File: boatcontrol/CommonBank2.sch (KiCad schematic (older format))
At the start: 29 parts, among them J5101 Conn_01x01_Male, J5102 TBP01R2W-508-08BE, J5103 Conn_01x01_Male, J5104 TBL008V-1000-02BE, J5105 TBP01R2W-508-08BE, J5106 Conn_01x01_Male, J5107 Conn_01x01_Male, J5108 TBL008V-1000-02BE, Q5101 IPP120P04P4L-03, U5101 MCP23017-E/SP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

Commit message: RPi scheme update done
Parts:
- JP5109, JP5110: value Jumper_NO_Small -> Jumper_NC_Small; symbol Device:Jumper_NO_Small -> Device:Jumper_NC_Small
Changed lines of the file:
@@
 Connection ~ 8150 2400
 $Comp
-L Device:Jumper_NO_Small JP?
+L Device:Jumper_NC_Small JP?
 U 1 1 61788453
 P 9600 5850
@@
 AR Path="/D1BB8DB4/61788453" Ref="JP5110"  Part="1"
 F 0 "JP5110" H 9600 5950 50  0000 C CNN
-F 1 "Jumper_NO_Small" H 9650 5750 50  0001 C CNN
+F 1 "Jumper_NC_Small" H 9650 5750 50  0001 C CNN
 F 2 "Connector_PinHeader_2.54mm:PinHeader_1x02_P2.54mm_Vertical" H 9600 5850 50  0001 C CNN
 F 3 "~" H 9600 5850 50  0001 C CNN
@@
 	9750 5850 9750 6000
 $Comp
-L Device:Jumper_NO_Small JP?
+L Device:Jumper_NC_Small JP?
 U 1 1 617AACB3
 P 9500 2150
@@
 AR Path="/D1BB8DB4/617AACB3" Ref="JP5109"  Part="1"
 F 0 "JP5109" H 9500 2250 50  0000 C CNN
-F 1 "Jumper_NO_Small" H 9550 2050 50  0001 C CNN
+F 1 "Jumper_NC_Small" H 9550 2050 50  0001 C CNN
 F 2 "Connector_PinHeader_2.54mm:PinHeader_1x02_P2.54mm_Vertical" H 9500 2150 50  0001 C CNN
 F 3 "~" H 9500 2150 50  0001 C CNN
@@
 Wire Wire Line
 	9600 2150 9650 2150
-Text Notes 7400 1100 0    50   ~ 0
-It's safe to run AC up to 277V 50/60hz and DC up to 24V on this circuit even though it's marked AC.\nThe main difference between this and the DC specific circuits  is track spacing and lack of any polarity protection.
+Text Notes 6700 850  0    50   ~ 0
+It's safe to run AC up to 277V 50/60hz and DC up to 24V on this circuit even though it's marked AC.\nThe main difference between this and the DC specific circuits is track spacing and lack of any polarity protection.
 $Comp
 L BoatControl:TBL008V-1000-02BE J?

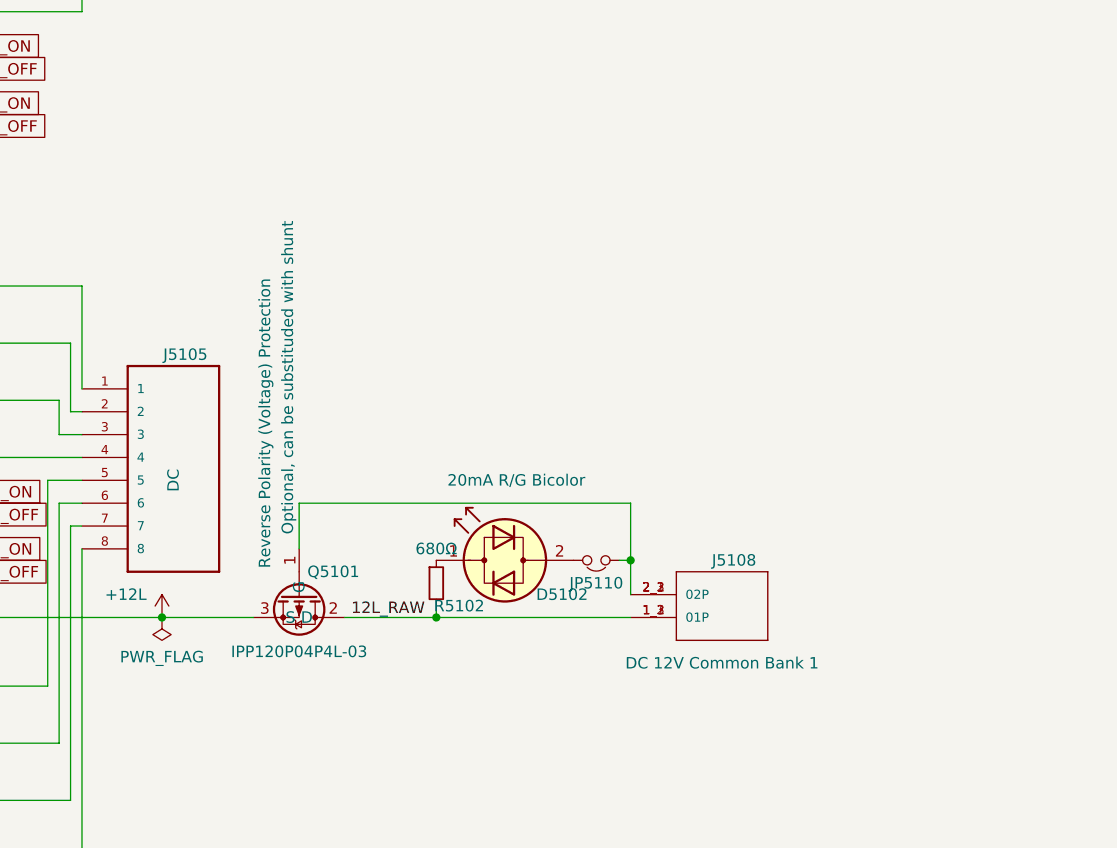
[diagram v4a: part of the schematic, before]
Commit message: Scale reverse polarity protection
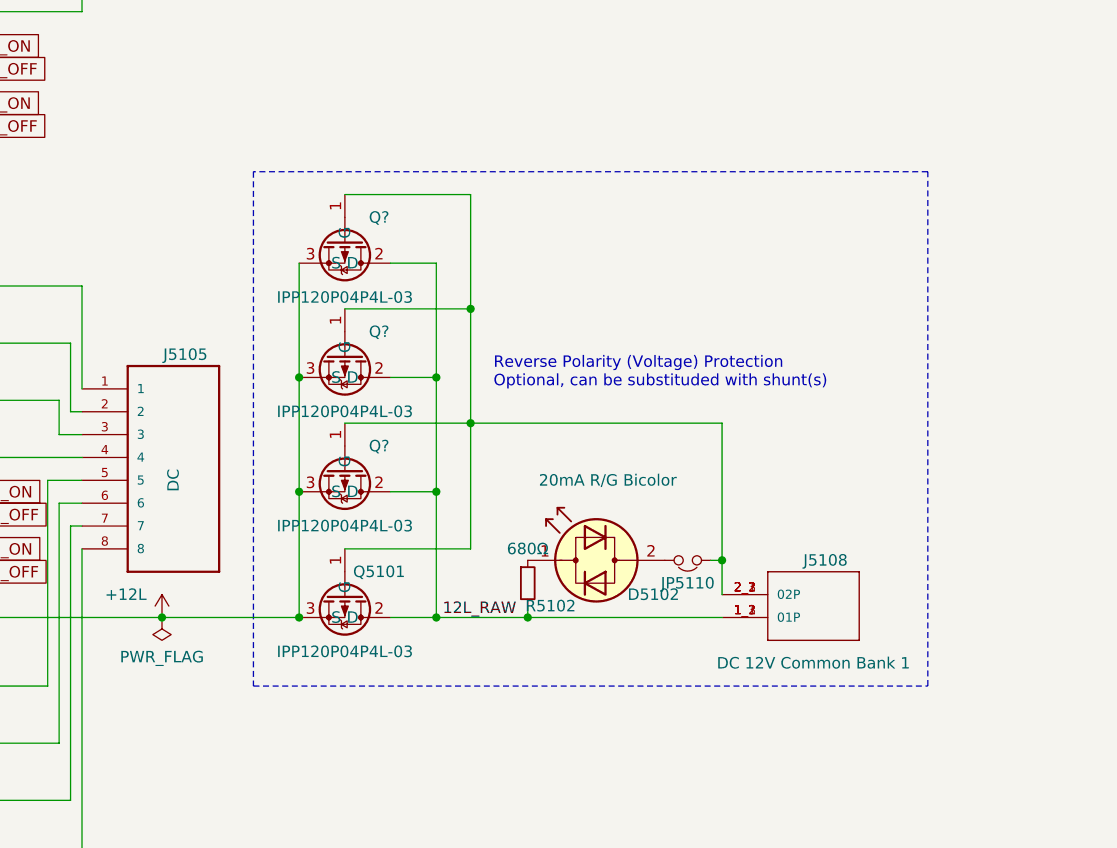
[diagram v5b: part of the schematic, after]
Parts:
- added Q? (x3): IPP120P04P4L-03, Package_TO_SOT_THT:TO-220-3_Vertical, symbol BoatControl:IPP120P04P4L-03
- Q5101: Note Optional, can be substituded with shunt -> (none); Purpose Reverse Polarity (Voltage) Protection -> (none)
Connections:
- net +12L: now also Q?.3 (S), Q?.3 (S), Q?.3 (S)
- net 12L_RAW: now also Q?.2 (D), Q?.2 (D), Q?.2 (D)
- net at J5108.2_1 (02P), J5108.2_2 (02P), J5108.2_3 (02P)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: now also Q?.1 (G), Q?.1 (G), Q?.1 (G)
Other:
- note added: "Reverse Polarity (Voltage) Protection\nOptional, can be substituded with shunt(s)"
- moved on the sheet: D5102, J5108, JP5110, Q5101, R5102

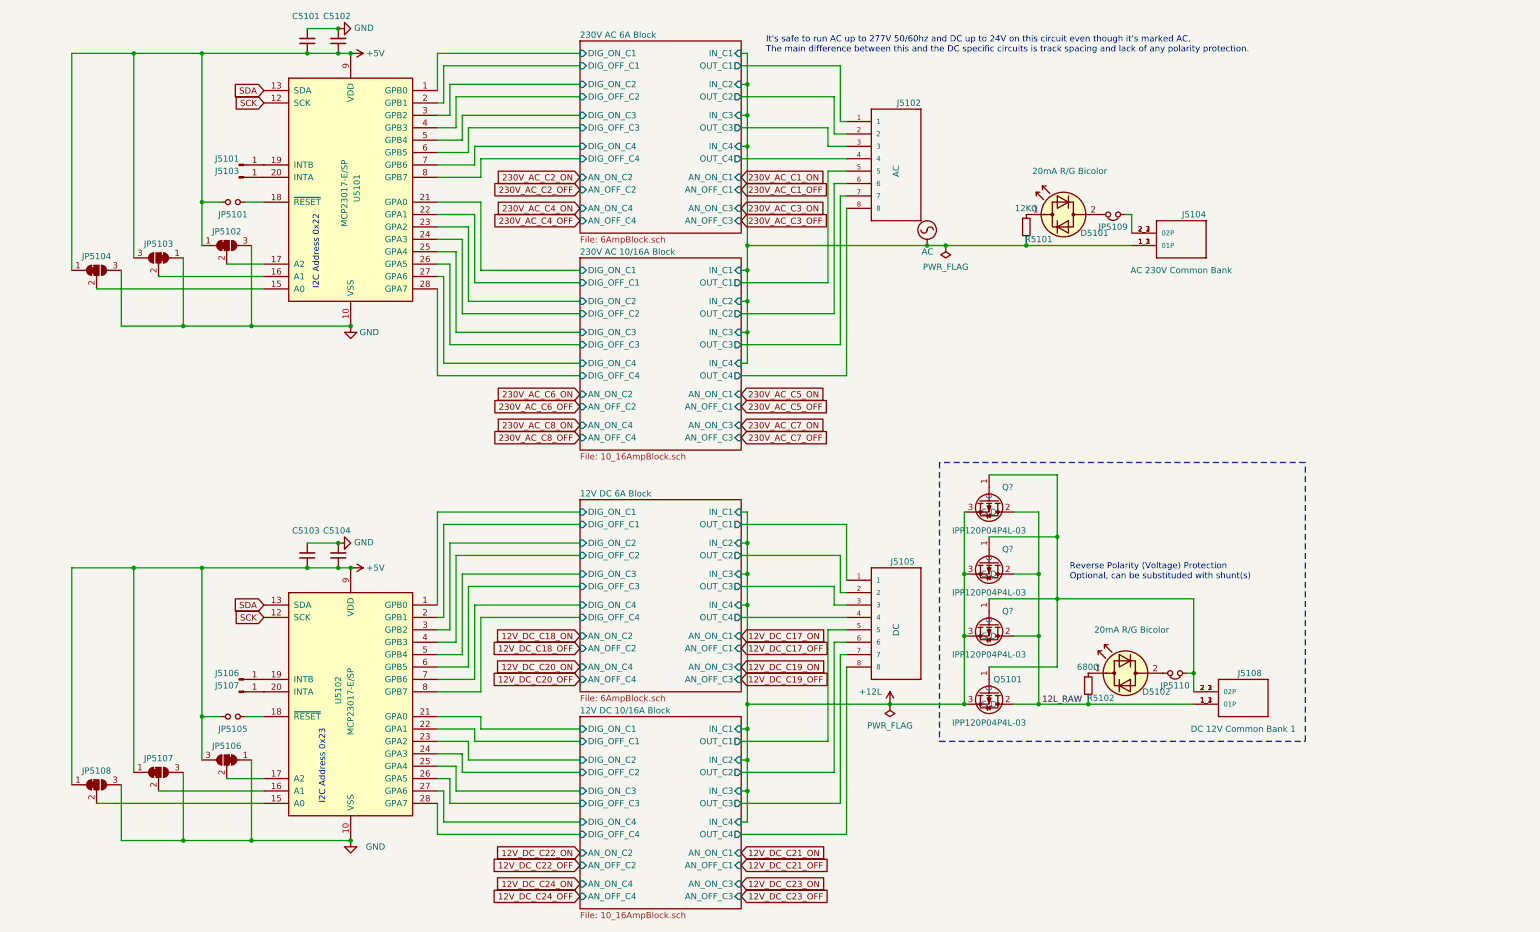
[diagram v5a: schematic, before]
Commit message: Add notes about power use of polarity protection
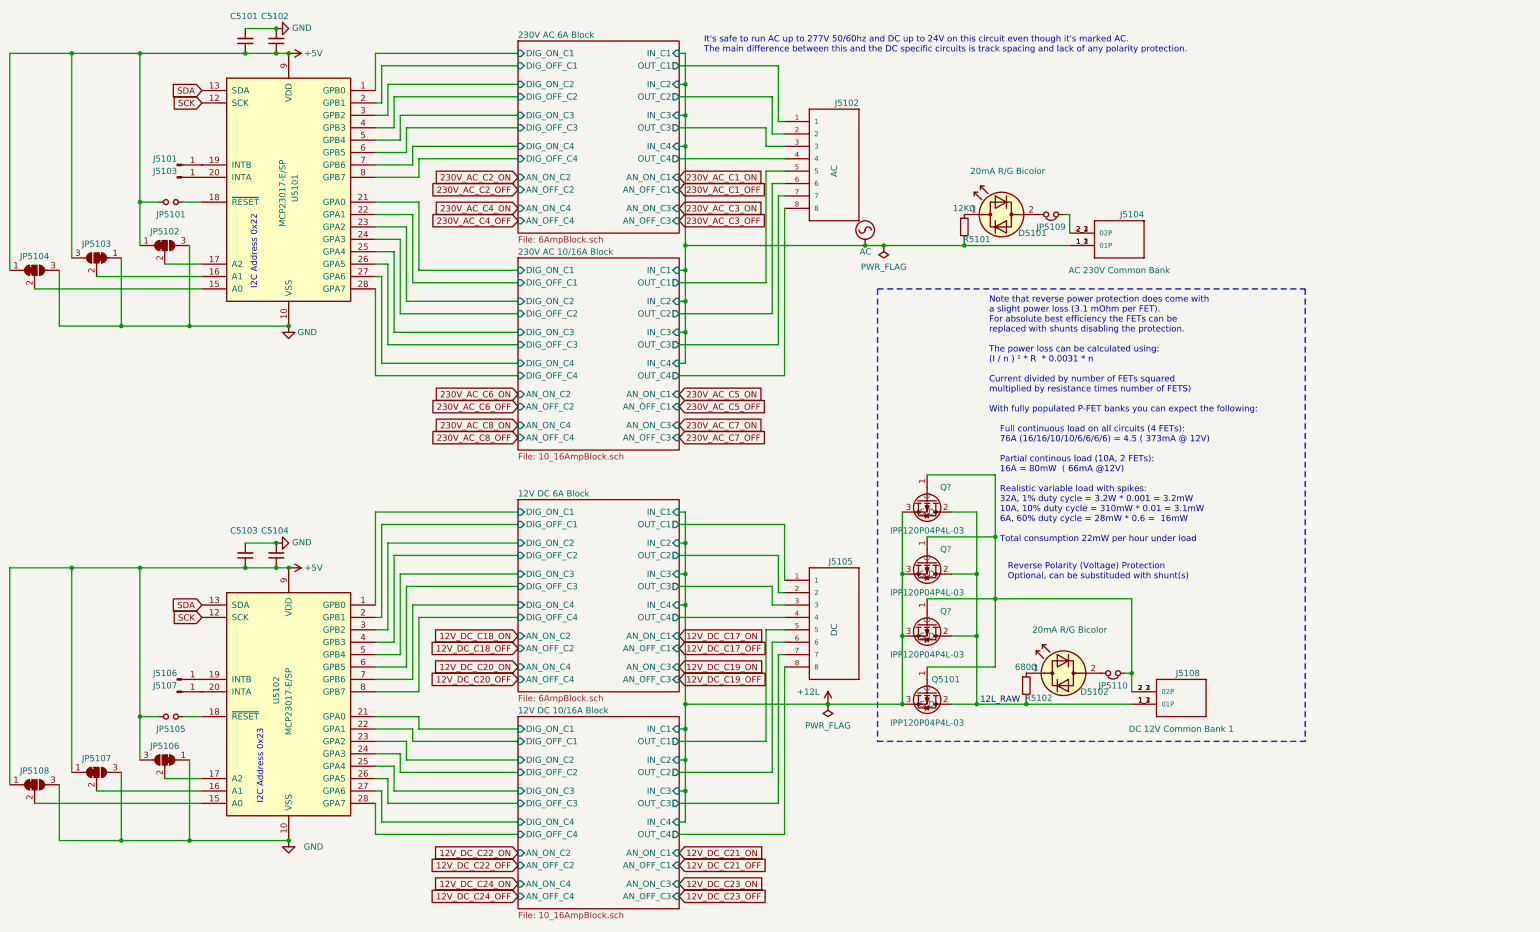
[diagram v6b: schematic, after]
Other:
- note added: "Note that reverse power protection does come with\na slight power loss (3.1 mOhm per FET).\nFor absolute best efficiency the FETs can be\nreplaced with shunts disabling the protection.\n\nThe power loss can be calculated using:\n(I / n ) ² * R * 0.0031 * n\n\nCurrent divided by number of FETs squared\nmultiplied by resistance times number of FETS) \n\nWith fully populated P-FET banks you can expe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"
- moved on the sheet: C5101, C5102, C5103, C5104, D5101, D5102, J5101, J5102, J5103, J5104, J5105, J5106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

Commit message: Cleanup
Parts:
- D5101, D5102: symbol Device:LED_Dual_2pin -> boatcontrol-rescue:LED_Dual_2pin-Device
- JP5101, JP5105: symbol Device:Jumper_NO_Small -> boatcontrol-rescue:Jumper_NO_Small-Device
- JP5102, JP5103, JP5104, JP5106, JP5107, JP5108: symbol Jumper:SolderJumper_3_Bridged12_Output -> boatcontrol-rescue:SolderJumper_3_Bridged12_Output-Jumper
- JP5109, JP5110: symbol Device:Jumper_NC_Small -> boatcontrol-rescue:Jumper_NC_Small-Device
- gave numbers to parts that had none: 3
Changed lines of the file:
@@
 $EndComp
 $Comp
-L Device:Jumper_NO_Small JP?
+L boatcontrol-rescue:Jumper_NO_Small-Device JP?
 U 1 1 D2B4FEF3
 P 1900 6200
@@
 Connection ~ 1500 7200
 $Comp
-L Device:Jumper_NO_Small JP?
+L boatcontrol-rescue:Jumper_NO_Small-Device JP?
 U 1 1 D1AAA2E7
 P 1900 2050
@@
 I2C Address 0x22
 $Comp
-L Jumper:SolderJumper_3_Bridged12_Output JP?
+L boatcontrol-rescue:SolderJumper_3_Bridged12_Output-Jumper JP?
 U 1 1 5F6B5DDA
 P 1300 2500
@@
 $EndComp
 $Comp
-L Jumper:SolderJumper_3_Bridged12_Output JP?
+L boatcontrol-rescue:SolderJumper_3_Bridged12_Output-Jumper JP?
 U 1 1 5F6B5DE6
 P 800 2600
@@
 $EndComp
 $Comp
-L Jumper:SolderJumper_3_Bridged12_Output JP?
+L boatcontrol-rescue:SolderJumper_3_Bridged12_Output-Jumper JP?
 U 1 1 5F6C92E8
 P 1850 2400
@@
 $EndComp
 $Comp
-L Jumper:SolderJumper_3_Bridged12_Output JP?
+L boatcontrol-rescue:SolderJumper_3_Bridged12_Output-Jumper JP?
 U 1 1 5F6ED611
 P 800 6750
@@
 $EndComp
 $Comp
-L Jumper:SolderJumper_3_Bridged12_Output JP?
+L boatcontrol-rescue:SolderJumper_3_Bridged12_Output-Jumper JP?
 U 1 1 5F6F4B4B
 P 1300 6650
@@
 $EndComp
 $Comp
-L Jumper:SolderJumper_3_Bridged12_Output JP?
+L boatcontrol-rescue:SolderJumper_3_Bridged12_Output-Jumper JP?
 U 1 1 5F6F5095
 P 1850 6550
@@
 $EndComp
 $Comp
-L Device:LED_Dual_2pin D?
+L boatcontrol-rescue:LED_Dual_2pin-Device D?
 U 1 1 600A5AB3
 P 9100 5850
@@
 AR Path="/D16552B4/600A5AB3" Ref="D?"  Part="1"
 AR Path="/D1BB8DB4/600A5AB3" Ref="D5102"  Part="1"
-F 0 "D5102" H 8850 5700 50  0000 C CNN
+F 0 "D5102" H 8900 6050 50  0000 C CNN
 F 1 "20mA R/G Bicolor" H 9050 6200 50  0000 C CNN
 F 2 "LED_THT:LED_D5.0mm" H 9100 5850 50  0001 C CNN
@@
 AR Path="/D16552B4/600A5ABC" Ref="R?"  Part="1"
 AR Path="/D1BB8DB4/600A5ABC" Ref="R5102"  Part="1"
-F 0 "R5102" H 8900 5850 50  0000 C CNN
+F 0 "R5102" H 8600 5950 50  0000 C CNN
 F 1 "680Ω" H 8800 6100 50  0000 C CNN
 F 2 "Resistor_THT:R_Axial_DIN0207_L6.3mm_D2.5mm_P7.62mm_Horizontal" H 8800 5950 50  0001 C CNN
@@
 $EndComp
 $Comp
-L Device:LED_Dual_2pin D?
+L boatcontrol-rescue:LED_Dual_2pin-Device D?
 U 1 1 60113E24
 P 8600 2150
@@
 AR Path="/D16552B4/60113E24" Ref="D?"  Part="1"
 AR Path="/D1BB8DB4/60113E24" Ref="D5101"  Part="1"
-F 0 "D5101" H 8350 2000 50  0000 C CNN
+F 0 "D5101" H 8400 2350 50  0000 C CNN
 F 1 "20mA R/G Bicolor" H 8550 2500 50  0000 C CNN
 F 2 "LED_THT:LED_D5.0mm" H 8600 2150 50  0001 C CNN
@@
 Connection ~ 7650 2400
 $Comp
-L Device:Jumper_NC_Small JP?
+L boatcontrol-rescue:Jumper_NC_Small-Device JP?
 U 1 1 61788453
 P 9500 5850
@@
 AR Path="/D16552B4/61788453" Ref="JP?"  Part="1"
 AR Path="/D1BB8DB4/61788453" Ref="JP5110"  Part="1"
-F 0 "JP5110" H 9500 5950 50  0000 C CNN
+F 0 "JP5110" H 9500 5800 50  0000 C CNN
 F 1 "Jumper_NC_Small" H 9550 5750 50  0001 C CNN
 F 2 "Connector_PinHeader_2.54mm:PinHeader_1x02_P2.54mm_Vertical" H 9500 5850 50  0001 C CNN
@@
 	9650 5850 9650 6000
 $Comp
-L Device:Jumper_NC_Small JP?
+L boatcontrol-rescue:Jumper_NC_Small-Device JP?
 U 1 1 617AACB3
 P 9000 2150
@@
 AR Path="/D16552B4/617AACB3" Ref="JP?"  Part="1"
 AR Path="/D1BB8DB4/617AACB3" Ref="JP5109"  Part="1"
-F 0 "JP5109" H 9000 2250 50  0000 C CNN
+F 0 "JP5109" H 9000 2100 50  0000 C CNN
 F 1 "Jumper_NC_Small" H 9050 2050 50  0001 C CNN
 F 2 "Connector_PinHeader_2.54mm:PinHeader_1x02_P2.54mm_Vertical" H 9000 2150 50  0001 C CNN
@@
 AR Path="/D16552B4/60113E2D" Ref="R?"  Part="1"
 AR Path="/D1BB8DB4/60113E2D" Ref="R5101"  Part="1"
-F 0 "R5101" H 8400 2150 50  0000 C CNN
+F 0 "R5101" H 8100 2250 50  0000 C CNN
 F 1 "12KΩ" H 8300 2400 50  0000 C CNN
 F 2 "Resistor_THT:R_Axial_DIN0207_L6.3mm_D2.5mm_P7.62mm_Horizontal" H 8300 2250 50  0001 C CNN
@@
 Reverse Polarity (Voltage) Protection\nOptional, can be substituded with shunt(s)
 $Comp
-L BoatControl:IPP120P04P4L-03 Q?
+L BoatControl:IPP120P04P4L-03 Q5102
 U 1 1 63CE5E8E
 P 8000 5550
-AR Path="/D1BB8DB4/63CE5E8E" Ref="Q?"  Part="1"
+AR Path="/D1BB8DB4/63CE5E8E" Ref="Q5102"  Part="1"
 AR Path="/D16552B4/5FA17F38/63CE5E8E" Ref="Q?"  Part="1"
-F 0 "Q?" V 7800 5700 50  0000 C CNN
+F 0 "Q5102" V 7800 5700 50  0000 C CNN
 F 1 "IPP120P04P4L-03" V 8150 5550 50  0000 C CNN
 F 2 "Package_TO_SOT_THT:TO-220-3_Vertical" H 7650 6100 50  0001 C CNN
@@
 $EndComp
 $Comp
-L BoatControl:IPP120P04P4L-03 Q?
+L BoatControl:IPP120P04P4L-03 Q5103
 U 1 1 63CF3938
 P 8000 5050
-AR Path="/D1BB8DB4/63CF3938" Ref="Q?"  Part="1"
+AR Path="/D1BB8DB4/63CF3938" Ref="Q5103"  Part="1"
 AR Path="/D16552B4/5FA17F38/63CF3938" Ref="Q?"  Part="1"
-F 0 "Q?" V 7800 5200 50  0000 C CNN
+F 0 "Q5103" V 7800 5200 50  0000 C CNN
 F 1 "IPP120P04P4L-03" V 8150 5050 50  0000 C CNN
 F 2 "Package_TO_SOT_THT:TO-220-3_Vertical" H 7650 5600 50  0001 C CNN
@@
 Connection ~ 8800 6100
 $Comp
-L BoatControl:IPP120P04P4L-03 Q?
+L BoatControl:IPP120P04P4L-03 Q5104
 U 1 1 63D20233
 P 8000 4550
-AR Path="/D1BB8DB4/63D20233" Ref="Q?"  Part="1"
+AR Path="/D1BB8DB4/63D20233" Ref="Q5104"  Part="1"
 AR Path="/D16552B4/5FA17F38/63D20233" Ref="Q?"  Part="1"
-F 0 "Q?" V 7800 4700 50  0000 C CNN
+F 0 "Q5104" V 7800 4700 50  0000 C CNN
 F 1 "IPP120P04P4L-03" V 8150 4550 50  0000 C CNN
 F 2 "Package_TO_SOT_THT:TO-220-3_Vertical" H 7650 5100 50  0001 C CNN
